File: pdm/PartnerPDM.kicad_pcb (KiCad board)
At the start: 2 copper layers, 0 parts

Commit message: Adds components
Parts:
- added BAT: 3.6V, Partner:Partner_Molex_Mega-Fit_76829-0106_2x03_P5.70mm_Vertical, F.Cu at (114.7, 39.9)
- added REF**: TerminalBlock_Phoenix_MKDS-1,5-2-5.00_1x02_P5mm_Horizontal, TerminalBlock_Phoenix:TerminalBlock_Phoenix_MKDS-1,5-2-5.08_1x02_P5.08mm_Horizontal, F.Cu at (125.1, 15.0)
- added REF**: TerminalBlock_Phoenix_MKDS-1,5-4-5.00_1x04_P5mm_Horizontal, TerminalBlock_Phoenix:TerminalBlock_Phoenix_MKDS-1,5-4-5.08_1x04_P5.08mm_Horizontal, F.Cu at (25.1, 14.7)
- added REF**: TerminalBlock_Phoenix_MKDS-1,5-4-5.00_1x04_P5mm_Horizontal, TerminalBlock_Phoenix:TerminalBlock_Phoenix_MKDS-1,5-4-5.08_1x04_P5.08mm_Horizontal, F.Cu at (45.0, 65.0)
- added REF**: TerminalBlock_Phoenix_MKDS-1,5-4-5.00_1x04_P5mm_Horizontal, TerminalBlock_Phoenix:TerminalBlock_Phoenix_MKDS-1,5-4-5.08_1x04_P5.08mm_Horizontal, F.Cu at (105.0, 65.0)
- added REF**: TerminalBlock_Phoenix_MKDS-1,5-4-5.00_1x04_P5mm_Horizontal, TerminalBlock_Phoenix:TerminalBlock_Phoenix_MKDS-1,5-4-5.08_1x04_P5.08mm_Horizontal, F.Cu at (25.0, 65.0)
- added REF**: TerminalBlock_Phoenix_MKDS-1,5-4-5.00_1x04_P5mm_Horizontal, TerminalBlock_Phoenix:TerminalBlock_Phoenix_MKDS-1,5-4-5.08_1x04_P5.08mm_Horizontal, F.Cu at (45.0, 90.0)
- added REF**: TerminalBlock_Phoenix_MKDS-1,5-4-5.00_1x04_P5mm_Horizontal, TerminalBlock_Phoenix:TerminalBlock_Phoenix_MKDS-1,5-4-5.08_1x04_P5.08mm_Horizontal, F.Cu at (105.0, 90.0)
- added REF**: TerminalBlock_Phoenix_MKDS-1,5-4-5.00_1x04_P5mm_Horizontal, TerminalBlock_Phoenix:TerminalBlock_Phoenix_MKDS-1,5-4-5.08_1x04_P5.08mm_Horizontal, F.Cu at (25.0, 40.3)
- added REF**: TerminalBlock_Phoenix_MKDS-1,5-4-5.00_1x04_P5mm_Horizontal, TerminalBlock_Phoenix:TerminalBlock_Phoenix_MKDS-1,5-4-5.08_1x04_P5.08mm_Horizontal, F.Cu at (105.0, 40.3)
- added REF**: TerminalBlock_Phoenix_MKDS-1,5-4-5.00_1x04_P5mm_Horizontal, TerminalBlock_Phoenix:TerminalBlock_Phoenix_MKDS-1,5-4-5.08_1x04_P5.08mm_Horizontal, F.Cu at (25.0, 90.0)
- added REF**: TerminalBlock_Phoenix_MKDS-1,5-4-5.00_1x04_P5mm_Horizontal, TerminalBlock_Phoenix:TerminalBlock_Phoenix_MKDS-1,5-4-5.08_1x04_P5.08mm_Horizontal, F.Cu at (65.1, 14.7)
- added REF**: TerminalBlock_Phoenix_MKDS-1,5-4-5.00_1x04_P5mm_Horizontal, TerminalBlock_Phoenix:TerminalBlock_Phoenix_MKDS-1,5-4-5.08_1x04_P5.08mm_Horizontal, F.Cu at (85.0, 65.0)
- added REF**: TerminalBlock_Phoenix_MKDS-1,5-4-5.00_1x04_P5mm_Horizontal, TerminalBlock_Phoenix:TerminalBlock_Phoenix_MKDS-1,5-4-5.08_1x04_P5.08mm_Horizontal, F.Cu at (45.0, 40.3)
- added REF**: TerminalBlock_Phoenix_MKDS-1,5-4-5.00_1x04_P5mm_Horizontal, TerminalBlock_Phoenix:TerminalBlock_Phoenix_MKDS-1,5-4-5.08_1x04_P5.08mm_Horizontal, F.Cu at (85.0, 90.0)
- added REF**: TerminalBlock_Phoenix_MKDS-1,5-4-5.00_1x04_P5mm_Horizontal, TerminalBlock_Phoenix:TerminalBlock_Phoenix_MKDS-1,5-4-5.08_1x04_P5.08mm_Horizontal, F.Cu at (65.0, 65.0)
- added REF**: TerminalBlock_Phoenix_MKDS-1,5-4-5.00_1x04_P5mm_Horizontal, TerminalBlock_Phoenix:TerminalBlock_Phoenix_MKDS-1,5-4-5.08_1x04_P5.08mm_Horizontal, F.Cu at (85.0, 40.3)
- added REF**: TerminalBlock_Phoenix_MKDS-1,5-4-5.00_1x04_P5mm_Horizontal, TerminalBlock_Phoenix:TerminalBlock_Phoenix_MKDS-1,5-4-5.08_1x04_P5.08mm_Horizontal, F.Cu at (65.0, 90.0)
- added REF**: TerminalBlock_Phoenix_MKDS-1,5-4-5.00_1x04_P5mm_Horizontal, TerminalBlock_Phoenix:TerminalBlock_Phoenix_MKDS-1,5-4-5.08_1x04_P5.08mm_Horizontal, F.Cu at (85.1, 14.7)
- added REF**: TerminalBlock_Phoenix_MKDS-1,5-4-5.00_1x04_P5mm_Horizontal, TerminalBlock_Phoenix:TerminalBlock_Phoenix_MKDS-1,5-4-5.08_1x04_P5.08mm_Horizontal, F.Cu at (105.1, 14.7)
- added REF**: TerminalBlock_Phoenix_MKDS-1,5-4-5.00_1x04_P5mm_Horizontal, TerminalBlock_Phoenix:TerminalBlock_Phoenix_MKDS-1,5-4-5.08_1x04_P5.08mm_Horizontal, F.Cu at (65.0, 40.3)
- added REF**: PinHeader_1x02_P2.54mm_Vertical, Connector_PinHeader_2.54mm:PinHeader_1x02_P2.54mm_Vertical, F.Cu at (122.5, 27.5)
- added REF**: TerminalBlock_Phoenix_MKDS-1,5-4-5.00_1x04_P5mm_Horizontal, TerminalBlock_Phoenix:TerminalBlock_Phoenix_MKDS-1,5-4-5.08_1x04_P5.08mm_Horizontal, F.Cu at (45.1, 14.7)
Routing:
- net (no net): track 0.00 -> 427.2 mm
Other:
- board outline added: 138 x 105 mm

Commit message: Updates PCB
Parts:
- moved BAT 40.1 mm to (113.6, 80.0)
- moved REF** 40.0 mm to (125.0, 55.0)
- moved REF** 38.4 mm to (121.2, 65.9)
- moved REF** 0.30 mm to (25.0, 40.0)
- moved REF** 0.30 mm to (105.0, 40.0)
- moved REF** 0.30 mm to (45.0, 40.0)
- moved REF** 0.30 mm to (85.0, 40.0)
- moved REF** 0.30 mm to (65.0, 40.0)
- moved REF** 0.30 mm to (25.1, 15.0)
- moved REF** 0.30 mm to (65.1, 15.0)
- moved REF** 0.30 mm to (85.1, 15.0)
- moved REF** 0.30 mm to (105.1, 15.0)
- moved REF** 0.30 mm to (45.1, 15.0)
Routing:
- net (no net): track 427.2 -> 380.0 mm

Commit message: PDM further dev
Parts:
- moved REF** 6.12 mm to (121.2, 72.0)
- moved REF** 6.12 mm to (125.0, 61.1)
- moved BAT 6.11 mm to (113.6, 86.1)
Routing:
- net (no net): track 380.0 -> 459.0 mm
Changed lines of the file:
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@@
   (net 0 "")
   (footprint "TerminalBlock_Phoenix:TerminalBlock_Phoenix_MKDS-1,5-2-5.08_1x02_P5.08mm_Horizontal" (layer "F.Cu")
-    (at 125 55 180)
+    (at 125 61.115 180)
     (descr "Terminal Block Phoenix MKDS-1,5-2-5.08, 2 pins, pitch 5.08mm, size 10.2x9.8mm^2, drill diamater 1.3mm, pad diameter 2.6mm, see http://www.farnell.com/datasheets/100425.pdf, script-generated using https://github.com/pointhi/kicad-footprint-generator/scripts/TerminalBlock_Phoenix")
     (tags "THT Terminal Block Phoenix MKDS-1,5-2-5.08 pitch 5.08mm size 10.2x9.8mm^2 drill 1.3mm pad 2.6mm")
@@
   )
   (footprint "Connector_PinHeader_2.54mm:PinHeader_1x02_P2.54mm_Vertical" (layer "F.Cu")
-    (at 121.22 65.91 90)
+    (at 121.22 72.025 90)
     (descr "Through hole straight pin header, 1x02, 2.54mm pitch, single row")
     (tags "Through hole pin header THT 1x02 2.54mm single row")
@@
   )
   (footprint "Partner:Partner_Molex_Mega-Fit_76829-0106_2x03_P5.70mm_Vertical" (layer "F.Cu")
-    (at 113.605 80 90)
+    (at 113.605 86.115 90)
     (descr "Molex Mega-Fit Power Connectors, 76829-0106 (compatible alternatives: 172065-0206, 172065-0306), 3 Pins per row (http://www.molex.com/pdm_docs/sd/768290102_sd.pdf), generated with kicad-footprint-generator")
     (tags "connector Molex Mega-Fit side entry")
@@
     (fp_line (start 7.62 17.78) (end 7.62 0)
       (stroke (width 0.1) (type solid)) (layer "F.Fab"))
-    (pad "1" thru_hole circle (at 0 0 90) (size 2.8 2.8) (drill 2) (layers "*.Cu" "*.Mask"))
-    (pad "2" thru_hole circle (at -5.08 17.78 90) (size 2.8 2.8) (drill 2) (layers "*.Cu" "*.Mask"))
-    (pad "3" thru_hole circle (at 5.08 17.78 90) (size 2.8 2.8) (drill 2) (layers "*.Cu" "*.Mask"))
+    (pad "1" thru_hole circle (at 0 0 90) (size 2.6 2.6) (drill 1.3) (layers "*.Cu" "*.Mask"))
+    (pad "2" thru_hole circle (at -5.08 17.78 90) (size 2.6 2.6) (drill 1.3) (layers "*.Cu" "*.Mask"))
+    (pad "3" thru_hole circle (at 5.08 17.78 90) (size 2.6 2.6) (drill 1.3) (layers "*.Cu" "*.Mask"))
     (model "${KICAD6_3DMODEL_DIR}/Connector_Molex.3dshapes/Molex_Mega-Fit_76829-0106_2x03_P5.70mm_Vertical.wrl"
       (offset (xyz 0 0 0))
@@
   (gr_circle (center 133 100) (end 134.5 100)
     (stroke (width 0.1) (type default)) (fill none) (layer "Edge.Cuts"))
-  (segment (start 10 40.003333) (end 105 40.003333) (width 1.8) (layer "B.Cu") (net 0))
-  (segment (start 10.08 15.005) (end 105.08 15.005) (width 1.8) (layer "B.Cu") (net 0))
-  (segment (start 10 90) (end 105 90) (width 1.8) (layer "B.Cu") (net 0))
-  (segment (start 10 65.001666) (end 105 65.001666) (width 1.8) (layer "B.Cu") (net 0))
-  (group "" (id e63ce1f0-d969-4a5a-a9a4-c171cbe7bd40)
-    (members
-      01815b91-213e-49c2-9a4e-88dbe9146a66
-      5e019705-667f-4f4f-89cc-3e5c7e4ece85
-      aa852e5b-30a3-44ef-bcf6-31628e905962
-    )
-  )
+  (segment (start 10 40.003333) (end 105 40.003333) (width 1.4) (layer "B.Cu") (net 0))
+  (segment (start 127.295 72.025) (end 131.385 76.115) (width 1.4) (layer "B.Cu") (net 0))
+  (segment (start 131.385 76.115) (end 131.385 67.5) (width 1.4) (layer "B.Cu") (net 0))
+  (segment (start 131.385 81.035) (end 131.385 76.115) (width 1.4) (layer "B.Cu") (net 0))
+  (segment (start 123.76 72.025) (end 127.295 72.025) (width 1.4) (layer "B.Cu") (net 0))
+  (segment (start 113.61 81.035) (end 113.61 86.11) (width 1.4) (layer "B.Cu") (net 0))
+  (segment (start 10.08 15.005) (end 105.08 15.005) (width 1.4) (layer "B.Cu") (net 0))
+  (segment (start 113.61 81.035) (end 113.61 76.115) (width 1.4) (layer "B.Cu") (net 0))
+  (segment (start 10 90) (end 105 90) (width 1.4) (layer "B.Cu") (net 0))
+  (segment (start 113.605 80.962413) (end 113.604685 80.962098) (width 0.25) (layer "B.Cu") (net 0))
+  (segment (start 117.7 72.025) (end 113.61 76.115) (width 1.4) (layer "B.Cu") (net 0))
+  (segment (start 113.61 67.505) (end 120 61.115) (width 1.4) (layer "B.Cu") (net 0))
+  (segment (start 113.61 86.11) (end 113.605 86.115) (width 0) (layer "B.Cu") (net 0))
+  (segment (start 10 65.001666) (end 105 65.001666) (width 1.4) (layer "B.Cu") (net 0))
+  (segment (start 121.22 72.025) (end 117.7 72.025) (width 1.4) (layer "B.Cu") (net 0))
+  (segment (start 131.385 91.195) (end 131.385 81.035) (width 1.4) (layer "B.Cu") (net 0))
+  (segment (start 113.61 76.115) (end 113.61 67.505) (width 1.4) (layer "B.Cu") (net 0))
+  (segment (start 131.385 67.5) (end 125 61.115) (width 1.4) (layer "B.Cu") (net 0))
   (group "" (id 2237db98-01a6-466a-99ef-7d4034d628f1)
     (members
@@
     )
   )
-  (group "" (id 36c2d1cf-10f5-4173-bc2c-243be78e4083)
-    (members
-      0d0cc018-0032-4682-9ebf-64b3432bbd4d
-      19df9f0e-3dd9-46a1-80aa-337912c36e26
-      5d2ce318-7adb-41e7-b5a6-dd37da717692
-      c1b3507b-dcb3-439c-a852-bb506b4655ae
-      cc88abbf-de21-44d5-8ce6-6f033368ea14
-      df21703d-0b67-4a32-b744-404dc3acbf6f
-    )
-  )

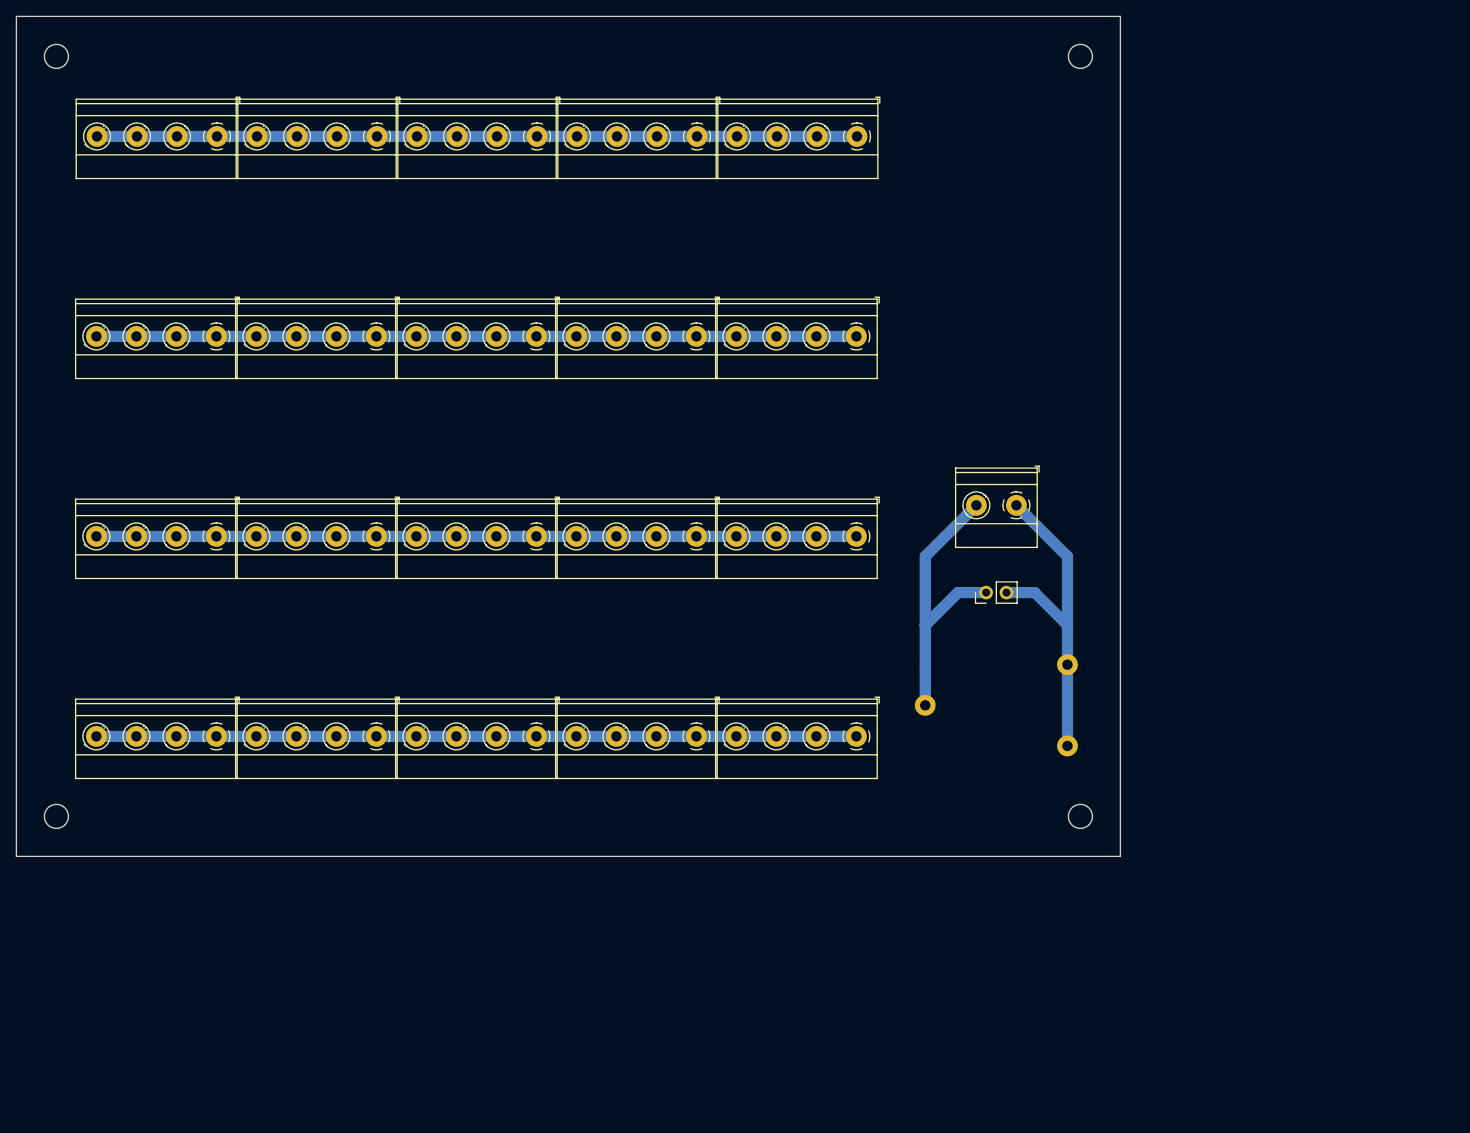
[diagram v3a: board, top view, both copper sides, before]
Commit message: Adds silkscreen
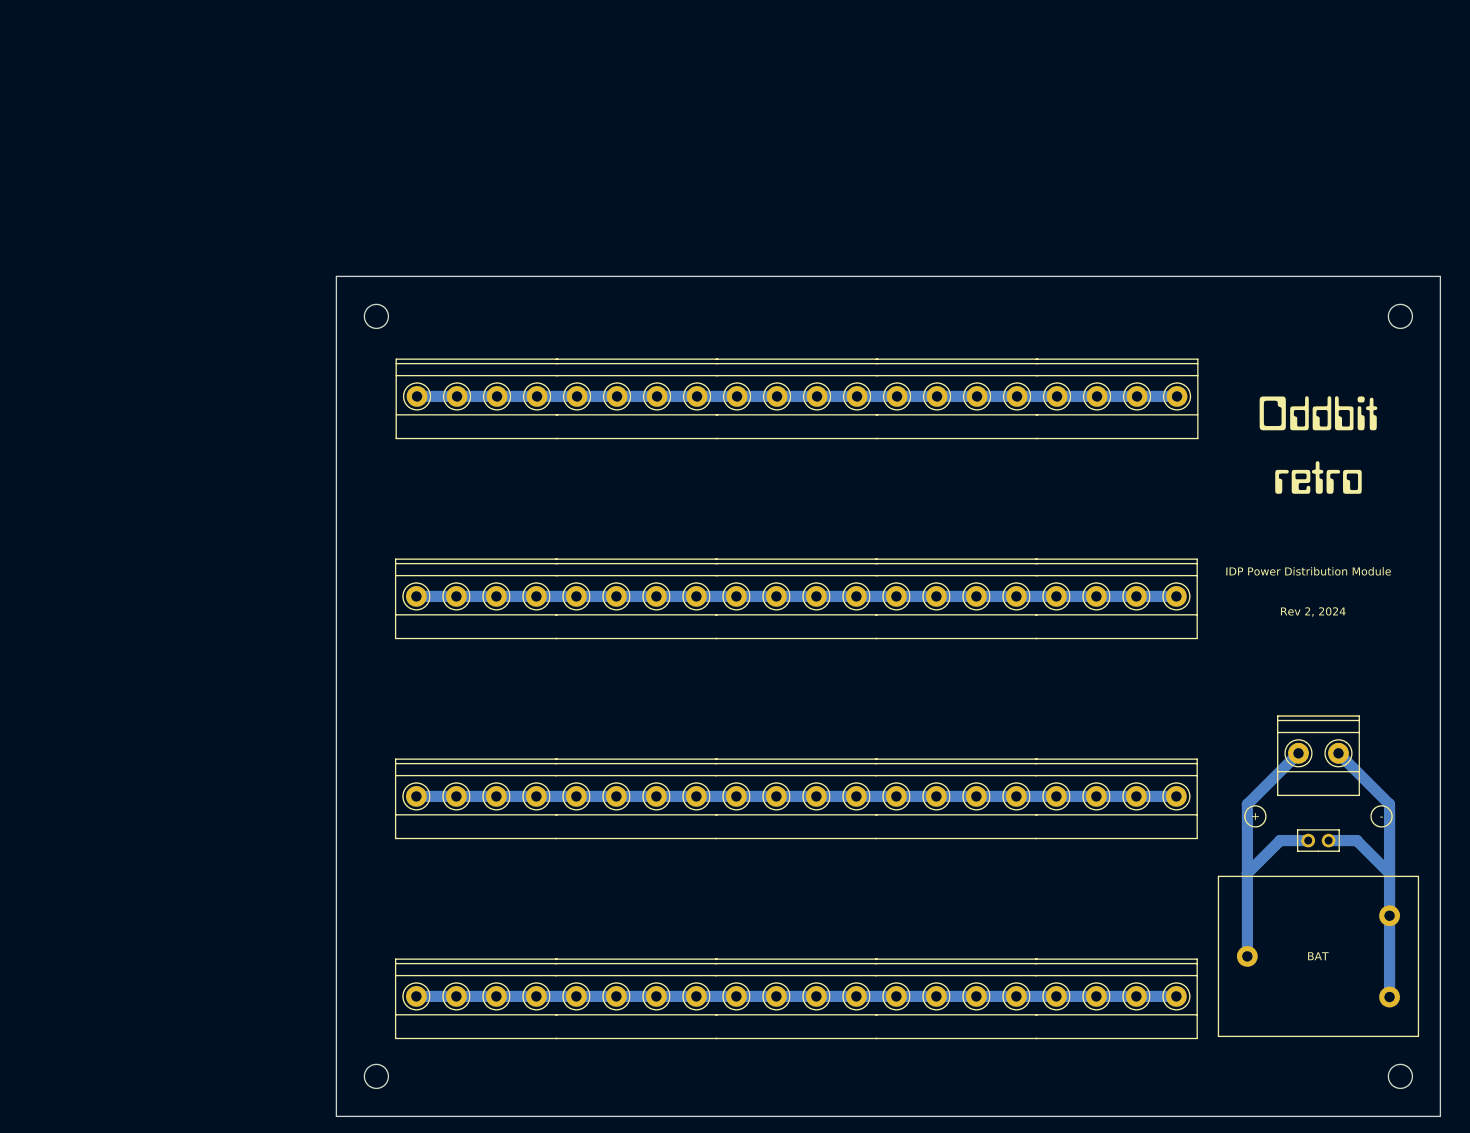
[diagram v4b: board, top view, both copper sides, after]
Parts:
- REF** (x20): footprint TerminalBlock_Phoenix:TerminalBlock_Phoenix_MKDS-1,5-4-5.08_1x04_P5.08mm_Horizontal -> Library:PARTNER_TerminalBlock_Phoenix_MKDS-1,5-4-5.08_1x04_P5.08mm_Horizontal
- moved REF** 51.5 mm to (145.1, 47.5)
- moved REF** 51.5 mm to (65.1, 47.5)
- moved REF** 51.5 mm to (85.0, 97.5)
- moved REF** 51.5 mm to (145.0, 97.5)
- moved REF** 51.5 mm to (65.0, 97.5)
- moved REF** 51.5 mm to (85.0, 122.5)
- moved REF** 51.5 mm to (145.0, 122.5)
- moved REF** 51.5 mm to (65.0, 72.5)
- moved REF** 51.5 mm to (145.0, 72.5)
- moved REF** 51.5 mm to (65.0, 122.5)
- moved REF** 51.5 mm to (105.1, 47.5)
- moved REF** 51.5 mm to (125.0, 97.5)
- moved REF** 51.5 mm to (85.0, 72.5)
- moved REF** 51.5 mm to (125.0, 122.5)
- moved REF** 51.5 mm to (105.0, 97.5)
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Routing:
- net (no net): track 459.0 -> 460.8 mm
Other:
- board text added: "+"
- board text added: "-"
- board text added: "BAT"
- board text added: "IDP Power Distribution Module"
- board text added: "Rev 2, 2024"

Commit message: Creates PDM GBR files
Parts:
- moved REF** 0.08 mm to (145.0, 47.5)
- moved REF** 0.08 mm to (65.0, 47.5)
- moved REF** 0.08 mm to (105.0, 47.5)
- moved REF** 0.08 mm to (125.0, 47.5)
- moved REF** 0.08 mm to (85.0, 47.5)
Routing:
- net (no net): track 460.8 -> 2130.8 mm
